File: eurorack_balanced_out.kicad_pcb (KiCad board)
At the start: 2 copper layers, 70 x 35 mm, 33 parts, among them J1 Conn_01x02, J2 Conn_01x02, J3 Conn_02x05_Odd_Even, J4 AudioJack3, J5 AudioJack3, U1 THAT1646W16, U2 THAT1646W16

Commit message: revision 0.1.1
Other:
- board text added: "Patchnut eurorack balanced output rev 0.1.1 https://github.com/mendelt/eurorack_balanced_out"
- board text removed: "Patchnut eurorack balanced output rev 0.1.0 https://github.com/mendelt/eurorack_balanced_out"

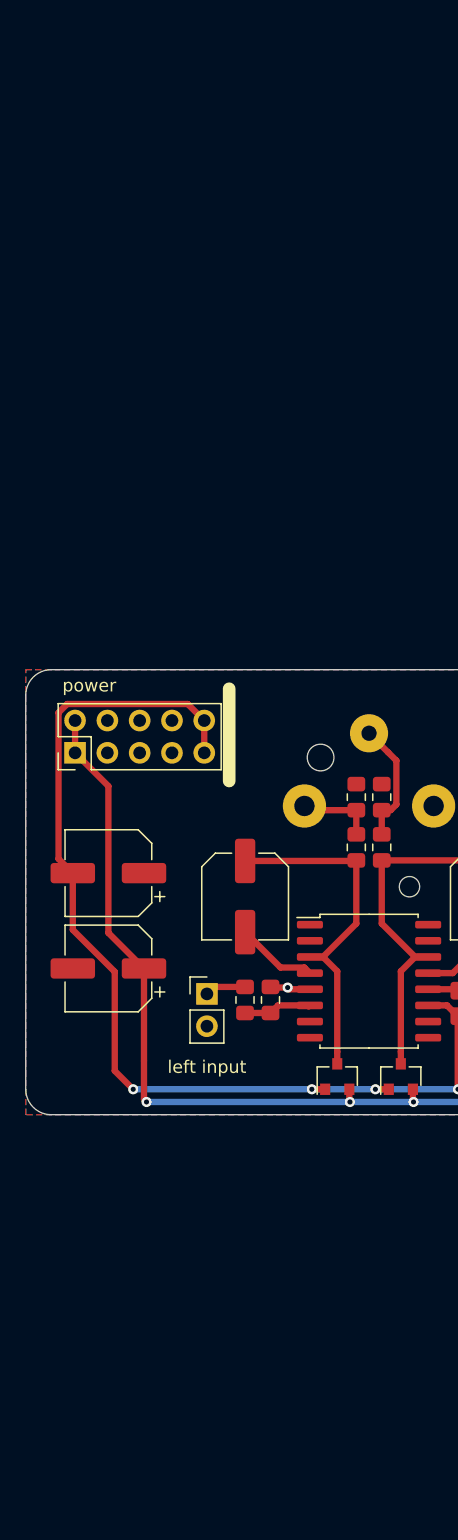
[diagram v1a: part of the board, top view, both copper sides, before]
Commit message: update schematic, add input buffer
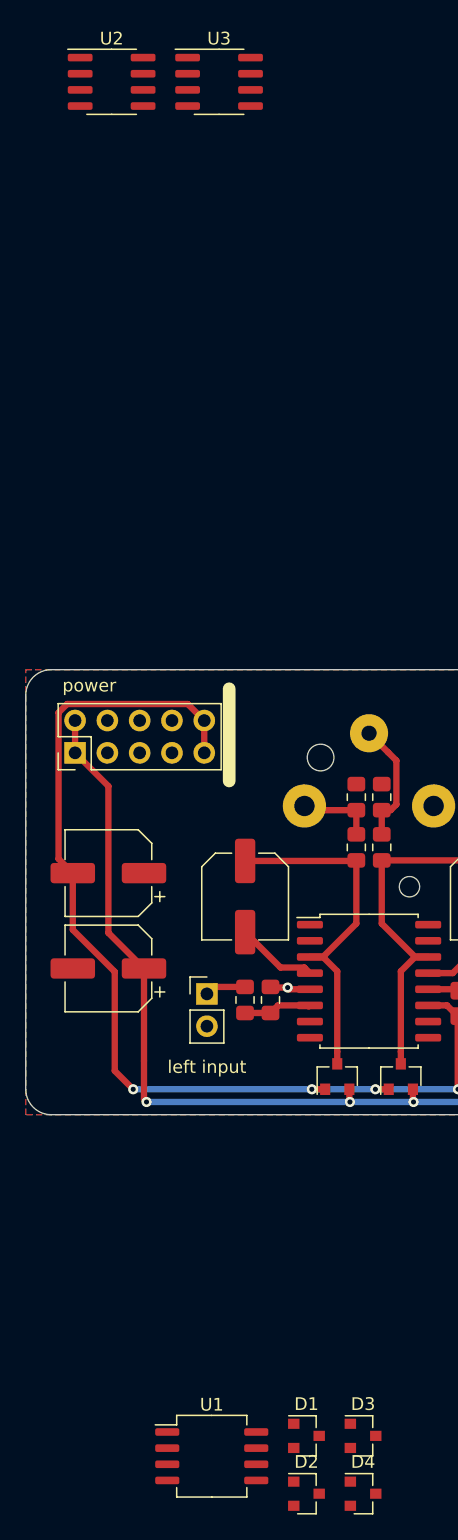
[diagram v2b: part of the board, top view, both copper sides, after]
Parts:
- added D1: BAV99, Package_TO_SOT_SMD:SOT-23, F.Cu at (132.1, 175.3)
- added D2: BAV99, Package_TO_SOT_SMD:SOT-23, F.Cu at (132.1, 179.8)
- added D3: BAV99, Package_TO_SOT_SMD:SOT-23, F.Cu at (136.5, 175.3)
- added D4: BAV99, Package_TO_SOT_SMD:SOT-23, F.Cu at (136.5, 179.8)
- added U1: TL072, Package_SO:SO-8_5.3x6.2mm_P1.27mm, F.Cu at (124.6, 176.9)
- added U2: THAT1646S08, Package_SO:SOIC-8_3.9x4.9mm_P1.27mm, F.Cu at (116.8, 68.8)
- added U3: THAT1646S08, Package_SO:SOIC-8_3.9x4.9mm_P1.27mm, F.Cu at (125.2, 68.8)
- renumbered C4 to C10, C13 to C11, C14 to C12, C9 to C13, C10 to C14, C11 to C15, C12 to C16, C3 to C9, D4 to D5, D2 to D6, J3 to J1, J1 to J2, J2 to J3, U1 to U2, U2 to U3
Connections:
- R1 pad 1: Net-(R1-Pad1) -> Net-(D1-Pad3)
- R2 pad 1: Net-(R2-Pad1) -> Net-(D2-Pad3)
- R3 pad 2: Net-(R1-Pad1) -> Net-(D1-Pad3)
- R4 pad 2: Net-(R2-Pad1) -> Net-(D2-Pad3)
- U2 pad 1: (no net) -> Net-(U2-Pad1)
- U2 pad 10: (no net) -> Net-(U2-Pad10)
- U2 pad 15: (no net) -> Net-(U2-Pad15)
- U2 pad 16: (no net) -> Net-(U2-Pad16)
- U2 pad 2: (no net) -> Net-(U2-Pad2)
- U2 pad 6: Net-(R1-Pad1) -> Net-(U1-Pad1)
- U2 pad 7: (no net) -> Net-(U2-Pad7)
- U2 pad 8: (no net) -> Net-(U2-Pad8)
- U2 pad 9: (no net) -> Net-(U2-Pad9)
- U3 pad 1: (no net) -> Net-(U3-Pad1)
- U3 pad 10: (no net) -> Net-(U3-Pad10)
- U3 pad 15: (no net) -> Net-(U3-Pad15)
- U3 pad 16: (no net) -> Net-(U3-Pad16)
- U3 pad 2: (no net) -> Net-(U3-Pad2)
- U3 pad 6: Net-(R2-Pad1) -> Net-(U1-Pad6)
- U3 pad 7: (no net) -> Net-(U3-Pad7)
- U3 pad 8: (no net) -> Net-(U3-Pad8)
- U3 pad 9: (no net) -> Net-(U3-Pad9)

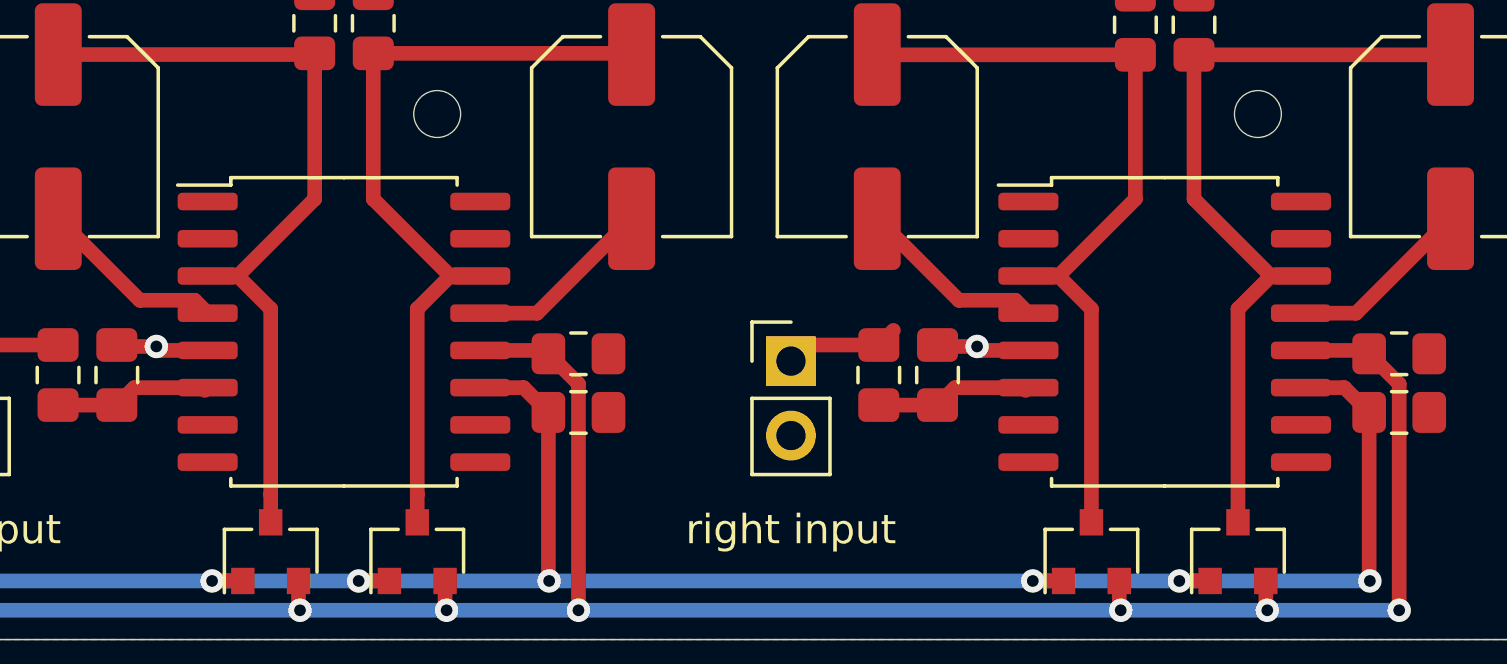
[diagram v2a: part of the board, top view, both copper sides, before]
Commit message: increase input impedance
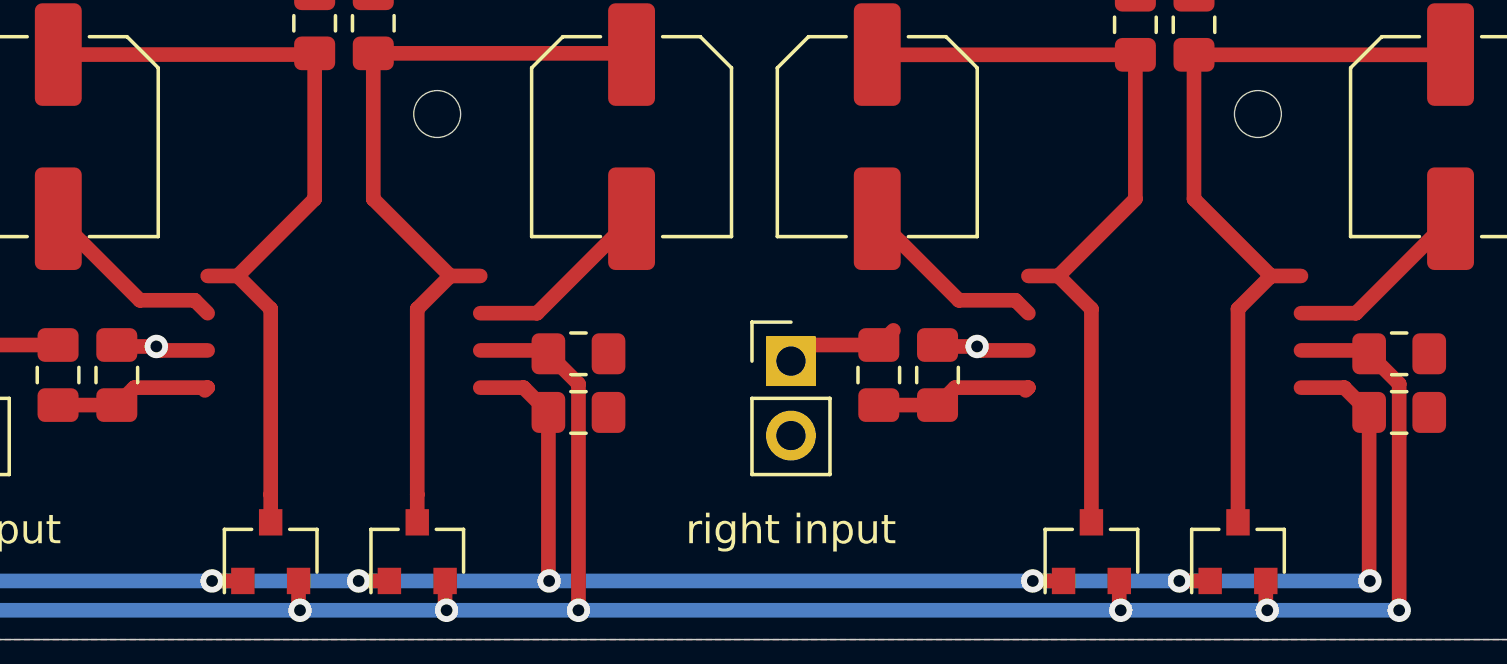
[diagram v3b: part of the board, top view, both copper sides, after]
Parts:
- removed the U2 at (137.0, 139.5)
- removed the U3 at (165.0, 139.5)
- R1, R2: value 3.9k -> 39k
- R3, R4: value 1.2k -> 12k
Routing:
- net Net-(R1-Pad1): track 5.48 -> 0.00 mm
- net Net-(D1-Pad3): track 0.00 -> 5.48 mm
- net Net-(R2-Pad1): track 5.48 -> 0.00 mm
- net Net-(D2-Pad3): track 0.00 -> 5.48 mm

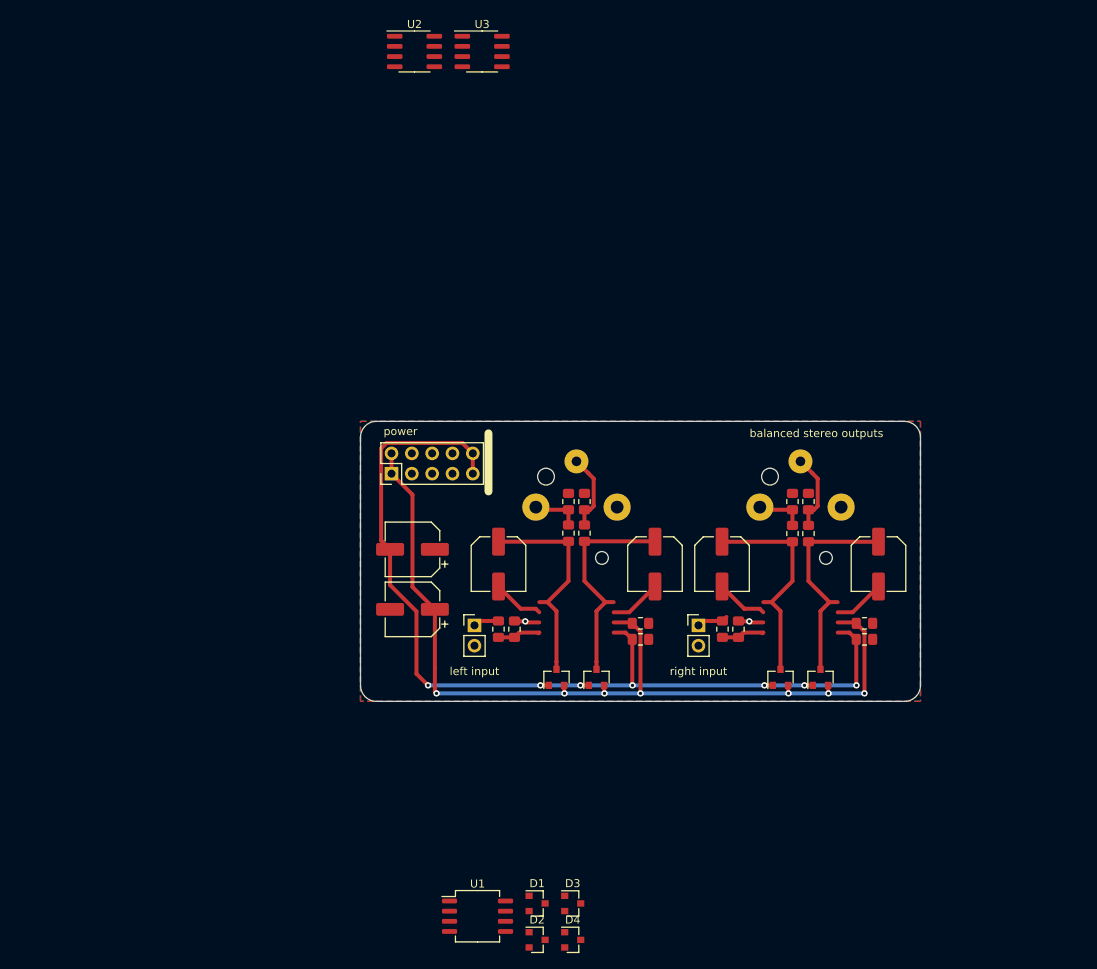
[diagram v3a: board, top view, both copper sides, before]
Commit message: set input and output jacks
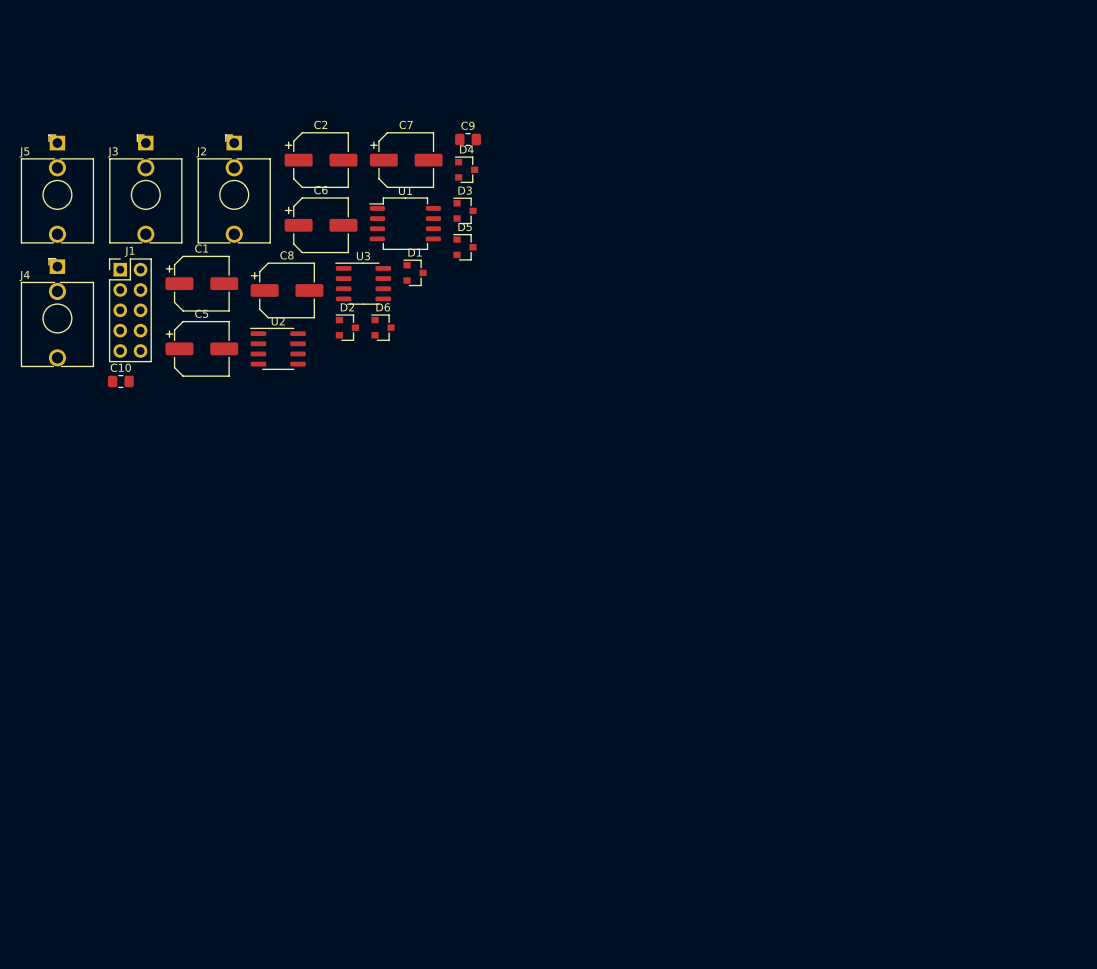
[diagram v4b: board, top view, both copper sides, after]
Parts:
- removed C11, C12: 100n, Capacitor_SMD:C_0805_2012Metric_Pad1.15x1.40mm_HandSolder
- removed C13, C14, C15, C16: 100p, Capacitor_SMD:C_0805_2012Metric_Pad1.15x1.40mm_HandSolder
- removed the D1 at (132.1, 175.3)
- removed the D1 at (134.5, 147.0)
- removed the D3 at (136.5, 175.3)
- removed the D3 at (139.5, 147.0)
- removed FB1, FB2, FB3, FB4: 600R @ 100Mhz, Resistor_SMD:R_0805_2012Metric_Pad1.15x1.40mm_HandSolder
- removed R1, R2: 39k, Resistor_SMD:R_0805_2012Metric_Pad1.15x1.40mm_HandSolder
- removed R3, R4: 12k, Resistor_SMD:R_0805_2012Metric_Pad1.15x1.40mm_HandSolder
- added D1: BAV99, Package_TO_SOT_SMD:SOT-23, F.Cu at (116.8, 96.4)
- added D3: BAV99, Package_TO_SOT_SMD:SOT-23, F.Cu at (123.1, 88.7)
- C10, C9: footprint Capacitor_SMD:C_0805_2012Metric_Pad1.15x1.40mm_HandSolder -> Capacitor_SMD:C_0805_2012Metric_Pad1.18x1.45mm_HandSolder
- J2, J3: value Conn_01x02 -> AudioJack2_SwitchT; footprint Connector_PinHeader_2.54mm:PinHeader_1x02_P2.54mm_Vertical -> Connector_Audio:Jack_3.5mm_QingPu_WQP-PJ398SM_Vertical_CircularHoles
- J4, J5: footprint Connector_Audio:Jack_6.35mm_Neutrik_NJ3FD-V_Vertical -> Connector_Audio:Jack_3.5mm_QingPu_WQP-PJ398SM_Vertical_CircularHoles; moved to F.Cu
- moved J5 101.0 mm to (72.1, 80.2), turned to 0 degrees
- moved D4 97.2 mm to (123.3, 83.5)
- moved J3 91.7 mm to (83.2, 80.2)
- moved U1 87.0 mm to (115.6, 90.3)
- moved D2 80.1 mm to (108.4, 103.3)
- moved C7 77.7 mm to (115.7, 82.3), turned to 0 degrees
- moved C10 72.5 mm to (80.0, 110.0)
- moved D5 69.7 mm to (123.1, 93.2), turned to 0 degrees
- moved J4 69.3 mm to (72.1, 95.7), turned to 0 degrees
- moved J2 67.4 mm to (94.2, 80.2)
- moved D6 66.2 mm to (112.8, 103.3), turned to 0 degrees
- moved C8 64.2 mm to (100.8, 98.6), turned to 0 degrees
- moved C9 64.2 mm to (123.5, 79.8), turned to 0 degrees
- moved C5 62.7 mm to (90.2, 105.9), turned to 0 degrees
- moved C2 50.0 mm to (105.1, 82.3), turned to 0 degrees
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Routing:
- net Vee: track 121.5 -> 0.00 mm, vias 7 -> 0
- net Vcc: track 113.0 -> 0.00 mm, vias 7 -> 0
- net Net-(C5-Pad1): track 27.4 -> 0.00 mm
- net Net-(C6-Pad1): track 27.3 -> 0.00 mm
- net Net-(C8-Pad1): track 27.3 -> 0.00 mm
- net Net-(C7-Pad1): track 27.3 -> 0.00 mm
- net Net-(C16-Pad1): track 9.78 -> 0.00 mm
- net Net-(C15-Pad1): track 9.73 -> 0.00 mm
- net Net-(C5-Pad2): track 6.50 -> 0.00 mm
- net Net-(C8-Pad2): track 6.49 -> 0.00 mm
- net Net-(C7-Pad2): track 6.44 -> 0.00 mm
- net Net-(C6-Pad2): track 6.43 -> 0.00 mm
- net GND: track 6.35 -> 0.00 mm, vias 2 -> 0
- net Net-(C14-Pad1): track 6.17 -> 0.00 mm
- net Net-(C13-Pad1): track 6.12 -> 0.00 mm
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- removed copper zone on B.Cu, net GND
- removed copper zone on F.Cu, net GND
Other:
- board outline removed
- board text removed: "Patchnut eurorack balanced output rev 0.1.1 https://github.com/mendelt/eurorack_balanced_out"
- board text removed: "balanced stereo outputs"
- board text removed: "left input"
- board text removed: "power"
- board text removed: "right input"
